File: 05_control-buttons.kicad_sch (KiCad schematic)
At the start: 9 parts, among them SW1 SW_Push, SW2 SW_Push, SW3 SW_Push, SW4 SW_Push

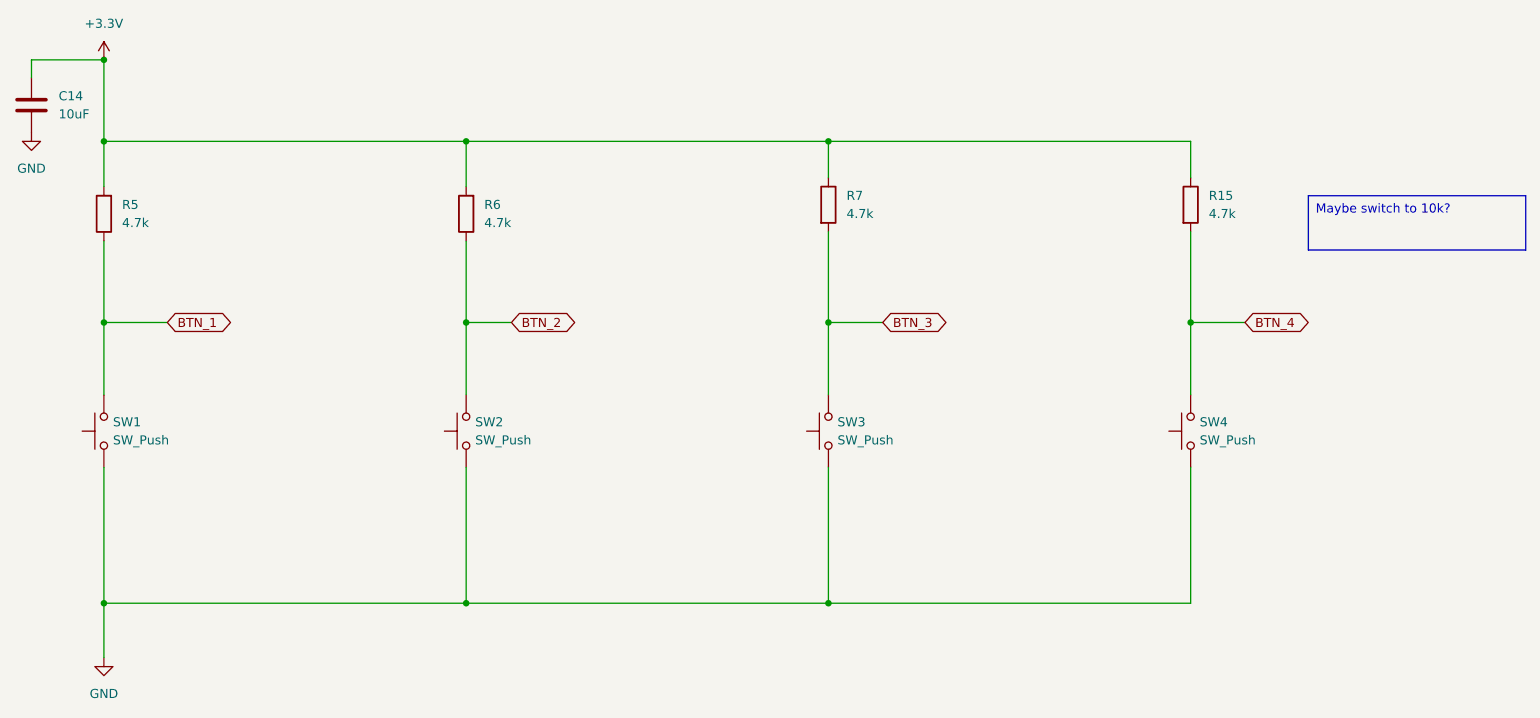
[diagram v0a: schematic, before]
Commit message: Redesigned SD Reader and Buttons
Signed-off-by: Anna-Lena Marx <anna-lena.marx@web.de>
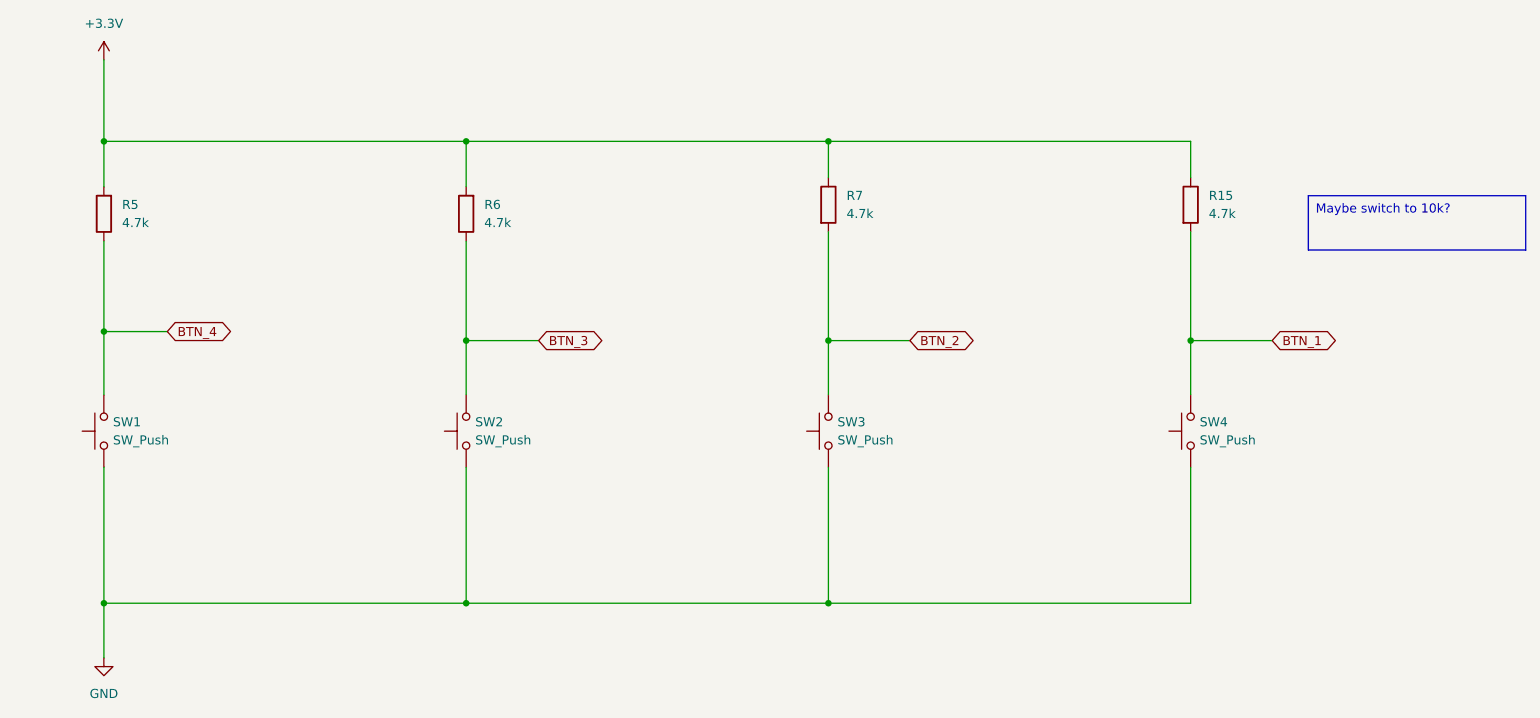
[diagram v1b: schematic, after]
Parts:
- removed C14: 10uF, Capacitor_SMD:C_1206_3216Metric_Pad1.33x1.80mm_HandSolder, symbol Device:C
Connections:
- net BTN_1: now also R15.2, SW4.2; no longer R5.1, SW1.2
- net BTN_2: now also R7.2, SW3.2; no longer R6.1, SW2.2
- net BTN_3: now also R6.1, SW2.2; no longer R7.2, SW3.2
- net BTN_4: now also R5.1, SW1.2; no longer R15.2, SW4.2
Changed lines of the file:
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@@
+	)
+	(junction
+		(at 173.99 86.36)
+		(diameter 0)
+		(color 0 0 0 0)
 	)
 	(junction
@@
 	)
 	(junction
-		(at 173.99 83.82)
-		(diameter 0)
-		(color 0 0 0 0)
-	)
-	(junction
-		(at 224.79 83.82)
-		(diameter 0)
-		(color 0 0 0 0)
-	)
-	(junction
 		(at 173.99 58.42)
 		(diameter 0)
@@
 	)
 	(junction
-		(at 123.19 83.82)
+		(at 72.39 85.09)
 		(diameter 0)
 		(color 0 0 0 0)
@@
 	)
 	(junction
-		(at 72.39 83.82)
-		(diameter 0)
-		(color 0 0 0 0)
-	)
-	(junction
-		(at 72.39 46.99)
+		(at 123.19 86.36)
+		(diameter 0)
+		(color 0 0 0 0)
+	)
+	(junction
+		(at 224.79 86.36)
 		(diameter 0)
 		(color 0 0 0 0)
@@
 	(wire
 		(pts
-			(xy 123.19 83.82) (xy 123.19 93.98)
+			(xy 123.19 72.39) (xy 123.19 86.36)
 		)
 		(stroke
@@
 	(wire
 		(pts
+			(xy 173.99 86.36) (xy 173.99 93.98)
+		)
+		(stroke
+			(width 0)
+			(type default)
+		)
+	)
+	(wire
+		(pts
 			(xy 72.39 46.99) (xy 72.39 58.42)
 		)
@@
 	(wire
 		(pts
+			(xy 224.79 86.36) (xy 224.79 93.98)
+		)
+		(stroke
+			(width 0)
+			(type default)
+		)
+	)
+	(wire
+		(pts
 			(xy 173.99 104.14) (xy 173.99 123.19)
 		)
@@
 	(wire
 		(pts
-			(xy 62.23 46.99) (xy 72.39 46.99)
-		)
-		(stroke
-			(width 0)
-			(type default)
-		)
-	)
-	(wire
-		(pts
-			(xy 123.19 83.82) (xy 129.54 83.82)
+			(xy 123.19 86.36) (xy 133.35 86.36)
 		)
 		(stroke
@@
 	(wire
 		(pts
-			(xy 62.23 46.99) (xy 62.23 49.53)
-		)
-		(stroke
-			(width 0)
-			(type default)
-		)
-	)
-	(wire
-		(pts
 			(xy 173.99 58.42) (xy 173.99 63.5)
 		)
@@
 	(wire
 		(pts
+			(xy 72.39 85.09) (xy 72.39 93.98)
+		)
+		(stroke
+			(width 0)
+			(type default)
+		)
+	)
+	(wire
+		(pts
+			(xy 123.19 86.36) (xy 123.19 93.98)
+		)
+		(stroke
+			(width 0)
+			(type default)
+		)
+	)
+	(wire
+		(pts
 			(xy 123.19 123.19) (xy 72.39 123.19)
 		)
@@
 	(wire
 		(pts
-			(xy 224.79 83.82) (xy 232.41 83.82)
-		)
-		(stroke
-			(width 0)
-			(type default)
-		)
-	)
-	(wire
-		(pts
 			(xy 123.19 58.42) (xy 123.19 64.77)
 		)
@@
 	(wire
 		(pts
-			(xy 72.39 83.82) (xy 72.39 72.39)
-		)
-		(stroke
-			(width 0)
-			(type default)
-		)
-	)
-	(wire
-		(pts
-			(xy 173.99 83.82) (xy 173.99 93.98)
-		)
-		(stroke
-			(width 0)
-			(type default)
-		)
-	)
-	(wire
-		(pts
-			(xy 224.79 71.12) (xy 224.79 83.82)
-		)
-		(stroke
-			(width 0)
-			(type default)
-		)
-	)
-	(wire
-		(pts
-			(xy 224.79 83.82) (xy 224.79 93.98)
-		)
-		(stroke
-			(width 0)
-			(type default)
-		)
-	)
-	(wire
-		(pts
-			(xy 72.39 93.98) (xy 72.39 83.82)
+			(xy 72.39 72.39) (xy 72.39 85.09)
+		)
+		(stroke
+			(width 0)
+			(type default)
+		)
+	)
+	(wire
+		(pts
+			(xy 224.79 71.12) (xy 224.79 86.36)
+		)
+		(stroke
+			(width 0)
+			(type default)
+		)
+	)
+	(wire
+		(pts
+			(xy 173.99 71.12) (xy 173.99 86.36)
 		)
 		(stroke
@@
 	(wire
 		(pts
-			(xy 173.99 83.82) (xy 181.61 83.82)
-		)
-		(stroke
-			(width 0)
-			(type default)
-		)
-	)
-	(wire
-		(pts
-			(xy 72.39 83.82) (xy 81.28 83.82)
-		)
-		(stroke
-			(width 0)
-			(type default)
-		)
-	)
-	(wire
-		(pts
-			(xy 173.99 71.12) (xy 173.99 83.82)
-		)
-		(stroke
-			(width 0)
-			(type default)
-		)
-	)
-	(wire
-		(pts
-			(xy 123.19 72.39) (xy 123.19 83.82)
-		)
-		(stroke
-			(width 0)
-			(type default)
-		)
-	)
-	(wire
-		(pts
 			(xy 72.39 123.19) (xy 72.39 130.81)
 		)
@@
 	(wire
 		(pts
+			(xy 185.42 86.36) (xy 173.99 86.36)
+		)
+		(stroke
+			(width 0)
+			(type default)
+		)
+	)
+	(wire
+		(pts
+			(xy 224.79 86.36) (xy 236.22 86.36)
+		)
+		(stroke
+			(width 0)
+			(type default)
+		)
+	)
+	(wire
+		(pts
 			(xy 72.39 58.42) (xy 72.39 64.77)
+		)
+		(stroke
+			(width 0)
+			(type default)
+		)
+	)
+	(wire
+		(pts
+			(xy 72.39 85.09) (xy 81.28 85.09)
 		)
 		(stroke
@@
 	(global_label "BTN_3"
 		(shape bidirectional)
-		(at 181.61 83.82 0)
+		(at 133.35 86.36 0)
 		(fields_autoplaced yes)
 		(effects
@@
 		)
 		(property "Intersheetrefs" "${INTERSHEET_REFS}"
-			(at 191.4517 83.82 0)
+			(at 143.1917 86.36 0)
 			(effects
 				(font
@@
 	(global_label "BTN_1"
 		(shape bidirectional)
-		(at 81.28 83.82 0)
+		(at 236.22 86.36 0)
 		(fields_autoplaced yes)
 		(effects
@@
 		)
 		(property "Intersheetrefs" "${INTERSHEET_REFS}"
-			(at 91.1217 83.82 0)
+			(at 246.0617 86.36 0)
 			(effects
 				(font
@@
 	(global_label "BTN_4"
 		(shape bidirectional)
-		(at 232.41 83.82 0)
+		(at 81.28 85.09 0)
 		(fields_autoplaced yes)
 		(effects
@@
 		)
 		(property "Intersheetrefs" "${INTERSHEET_REFS}"
-			(at 242.2517 83.82 0)
+			(at 91.1217 85.09 0)
 			(effects
 				(font
@@
 	(global_label "BTN_2"
 		(shape bidirectional)
-		(at 129.54 83.82 0)
+		(at 185.42 86.36 0)
 		(fields_autoplaced yes)
 		(effects
@@
 		)
 		(property "Intersheetrefs" "${INTERSHEET_REFS}"
-			(at 139.3817 83.82 0)
+			(at 195.2617 86.36 0)
 			(effects
 				(font
@@
 				)
 				(justify left)
-			)
-		)
-	)
-	(symbol
-		(lib_id "Device:C")
-		(at 62.23 53.34 180)
-		(unit 1)
-		(exclude_from_sim no)
-		(in_bom yes)
-		(on_board yes)
-		(dnp no)
-		(fields_autoplaced yes)
-		(property "Reference" "C14"
-			(at 66.04 52.0699 0)
-			(effects
-				(font
-					(size 1.27 1.27)
-				)
-				(justify right)
-			)
-		)
-		(property "Value" "10uF"
-			(at 66.04 54.6099 0)
-			(effects
-				(font
-					(size 1.27 1.27)
-				)
-				(justify right)
-			)
-		)
-		(property "Footprint" "Capacitor_SMD:C_1206_3216Metric_Pad1.33x1.80mm_HandSolder"
-			(at 61.2648 49.53 0)
-			(effects
-				(font
-					(size 1.27 1.27)
-				)
-				(hide yes)
-			)
-		)
-		(property "Datasheet" "~"
-			(at 62.23 53.34 0)
-			(effects
-				(font
-					(size 1.27 1.27)
-				)
-				(hide yes)
-			)
-		)
-		(property "Description" "Unpolarized capacitor"
-			(at 62.23 53.34 0)
-			(effects
-				(font
-					(size 1.27 1.27)
-				)
-				(hide yes)
-			)
-		)
-		(pin "2"
-		)
-		(pin "1"
-		)
-		(instances
-			(project ""
-				(path "/ec954637-2a8b-4662-b4a1-f88107f11cb0/33ac9274-8ec9-4374-b845-560e6893b431"
-					(reference "C14")
-					(unit 1)
-				)
 			)
 		)
@@
 					(unit 1)
 				)
-			)
-		)
-	)
-	(symbol
-		(lib_id "power:GND")
-		(at 62.23 57.15 0)
-		(unit 1)
-		(exclude_from_sim no)
-		(in_bom yes)
-		(on_board yes)
-		(dnp no)
-		(fields_autoplaced yes)
-		(property "Reference" "#PWR033"
-			(at 62.23 63.5 0)
-			(effects
-				(font
-					(size 1.27 1.27)
-				)
-				(hide yes)
-			)
-		)
-		(property "Value" "GND"
-			(at 62.23 62.23 0)
-			(effects
-				(font
-					(size 1.27 1.27)
-				)
-			)
-		)
-		(property "Footprint" ""
-			(at 62.23 57.15 0)
-			(effects
-				(font
-					(size 1.27 1.27)
-				)
-				(hide yes)
-			)
-		)
-		(property "Datasheet" ""
-			(at 62.23 57.15 0)
-			(effects
-				(font
-					(size 1.27 1.27)
-				)
-				(hide yes)
-			)
-		)
-		(property "Description" "Power symbol creates a global label with name \"GND\" , ground"
-			(at 62.23 57.15 0)
-			(effects
-				(font
-					(size 1.27 1.27)
-				)
-				(hide yes)
-			)
-		)
-		(pin "1"
-		)
-		(instances
-			(project ""
-				(path "/ec954637-2a8b-4662-b4a1-f88107f11cb0/33ac9274-8ec9-4374-b845-560e6893b431"
-					(reference "#PWR033")
-					(unit 1)
-				)

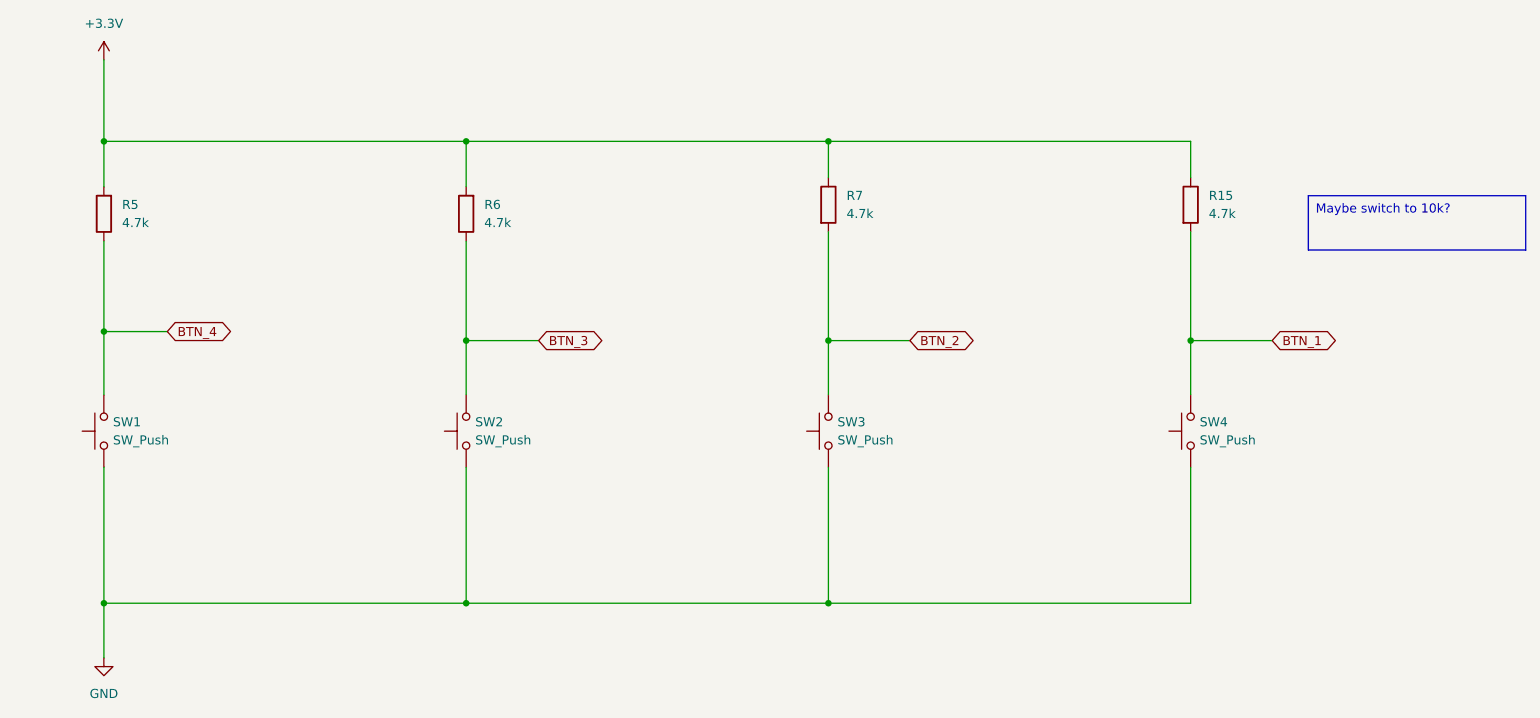
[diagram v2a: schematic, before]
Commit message: updated some values after testing out tuning details
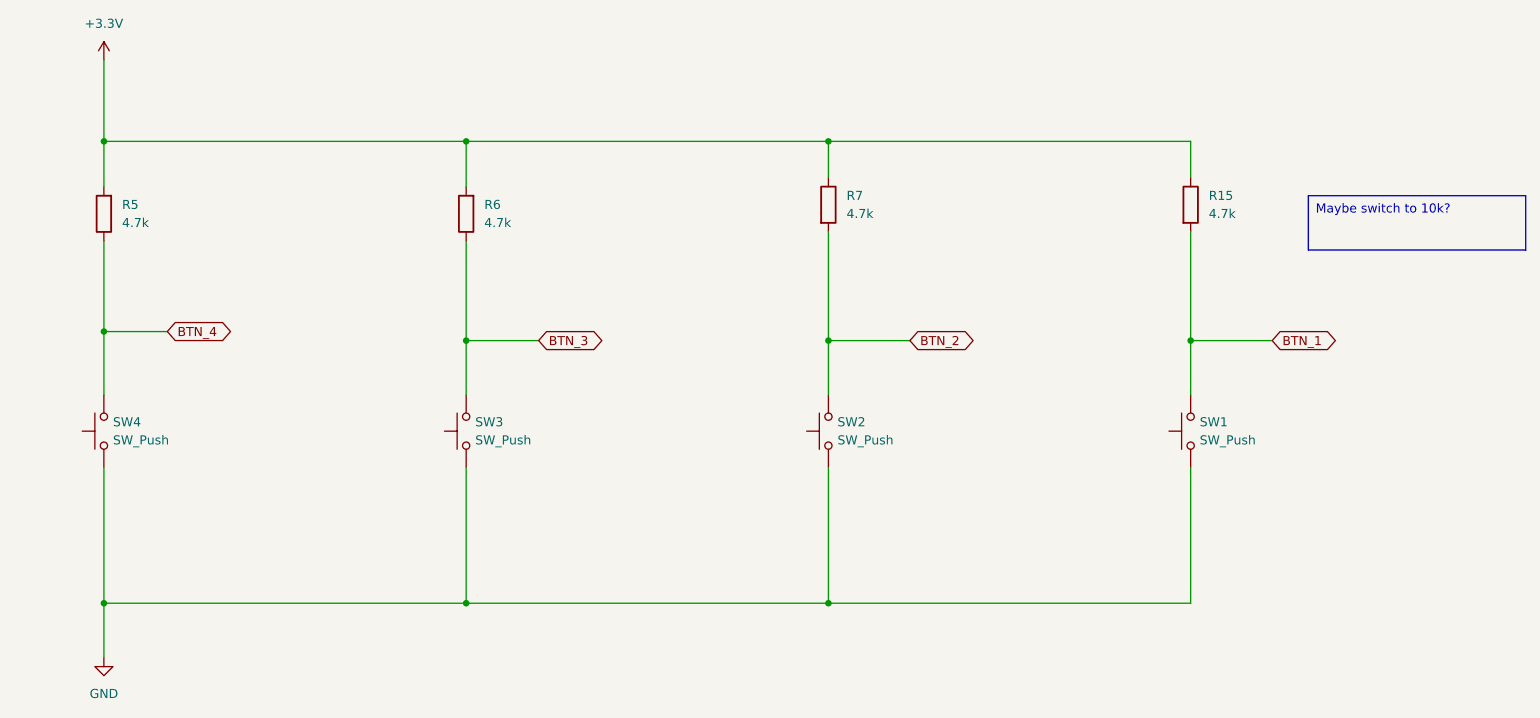
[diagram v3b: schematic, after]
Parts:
- renumbered SW4 to SW1, SW3 to SW2, SW2 to SW3, SW1 to SW4
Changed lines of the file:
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@@
 		(dnp no)
 		(fields_autoplaced yes)
-		(property "Reference" "SW2"
+		(property "Reference" "SW3"
 			(at 124.46 97.7899 90)
 			(effects
@@
 			(project "ZEReader-Pico"
 				(path "/ec954637-2a8b-4662-b4a1-f88107f11cb0/33ac9274-8ec9-4374-b845-560e6893b431"
-					(reference "SW2")
+					(reference "SW3")
 					(unit 1)
 				)
@@
 		(dnp no)
 		(fields_autoplaced yes)
-		(property "Reference" "SW3"
+		(property "Reference" "SW2"
 			(at 175.26 97.7899 90)
 			(effects
@@
 			(project "ZEReader-Pico"
 				(path "/ec954637-2a8b-4662-b4a1-f88107f11cb0/33ac9274-8ec9-4374-b845-560e6893b431"
-					(reference "SW3")
+					(reference "SW2")
 					(unit 1)
 				)
@@
 		(dnp no)
 		(fields_autoplaced yes)
-		(property "Reference" "SW4"
+		(property "Reference" "SW1"
 			(at 226.06 97.7899 90)
 			(effects
@@
 			(project "ZEReader-Pico"
 				(path "/ec954637-2a8b-4662-b4a1-f88107f11cb0/33ac9274-8ec9-4374-b845-560e6893b431"
-					(reference "SW4")
+					(reference "SW1")
 					(unit 1)
 				)
@@
 		(dnp no)
 		(fields_autoplaced yes)
-		(property "Reference" "SW1"
+		(property "Reference" "SW4"
 			(at 73.66 97.7899 90)
 			(effects
@@
 			(project ""
 				(path "/ec954637-2a8b-4662-b4a1-f88107f11cb0/33ac9274-8ec9-4374-b845-560e6893b431"
-					(reference "SW1")
-					(unit 1)
-				)
+					(reference "SW4")
+					(unit 1)
+				)
